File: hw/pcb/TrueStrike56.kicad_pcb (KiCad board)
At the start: 2 copper layers, 278.9 x 138.4 mm, 202 parts, among them SW1 SW_Push, U1 ProMicro, U10 4053, U2 74HC4051, U3 74HC4051, U4 74HC4051, U5 74HC4051, U6 74HC4051, U7 74HC4051, U8 74HC4051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

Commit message: Add mounting holes and plates, MCU cover
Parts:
- added REF**: MountingHole_3.5mm, MountingHole:MountingHole_3.5mm, F.Cu at (112.0, 58.3)
- added REF**: MountingHole_3.5mm, MountingHole:MountingHole_3.5mm, F.Cu at (250.3, 78.7)
- added REF**: MountingHole_3.5mm, MountingHole:MountingHole_3.5mm, F.Cu at (323.6, 58.3)
- added REF**: MountingHole_3.5mm, MountingHole:MountingHole_3.5mm, F.Cu at (162.2, 134.6)
- added REF**: MountingHole_3.5mm, MountingHole:MountingHole_3.5mm, F.Cu at (273.4, 134.6)
- added REF**: MountingHole_3.5mm, MountingHole:MountingHole_3.5mm, F.Cu at (100.5, 117.7)
- added REF**: MountingHole_3.5mm, MountingHole:MountingHole_3.5mm, F.Cu at (335.2, 117.7)
- added REF**: MountingHole_3.5mm, MountingHole:MountingHole_3.5mm, F.Cu at (185.3, 78.7)

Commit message: Add logo+model name+rev #, set LCSC Part # for PCBA order
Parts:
- added G***: LOGO, LOGO, B.Cu at (319.0, 119.1)
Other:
- board text added: "Rev.1"
- board text added: "TrueStrike56"

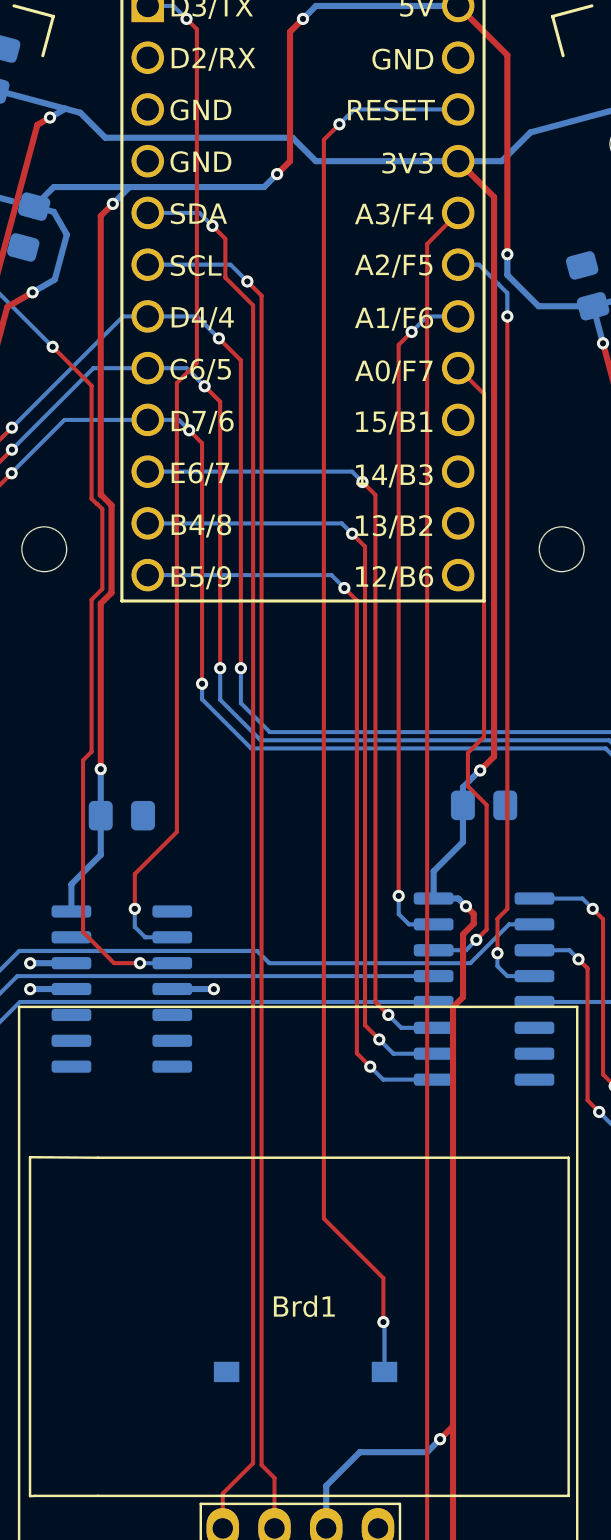
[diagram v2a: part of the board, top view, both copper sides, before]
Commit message: Update PCB and production files for PCBA
Changed RESET tactile switch to JLCPCB PCBA compatible part
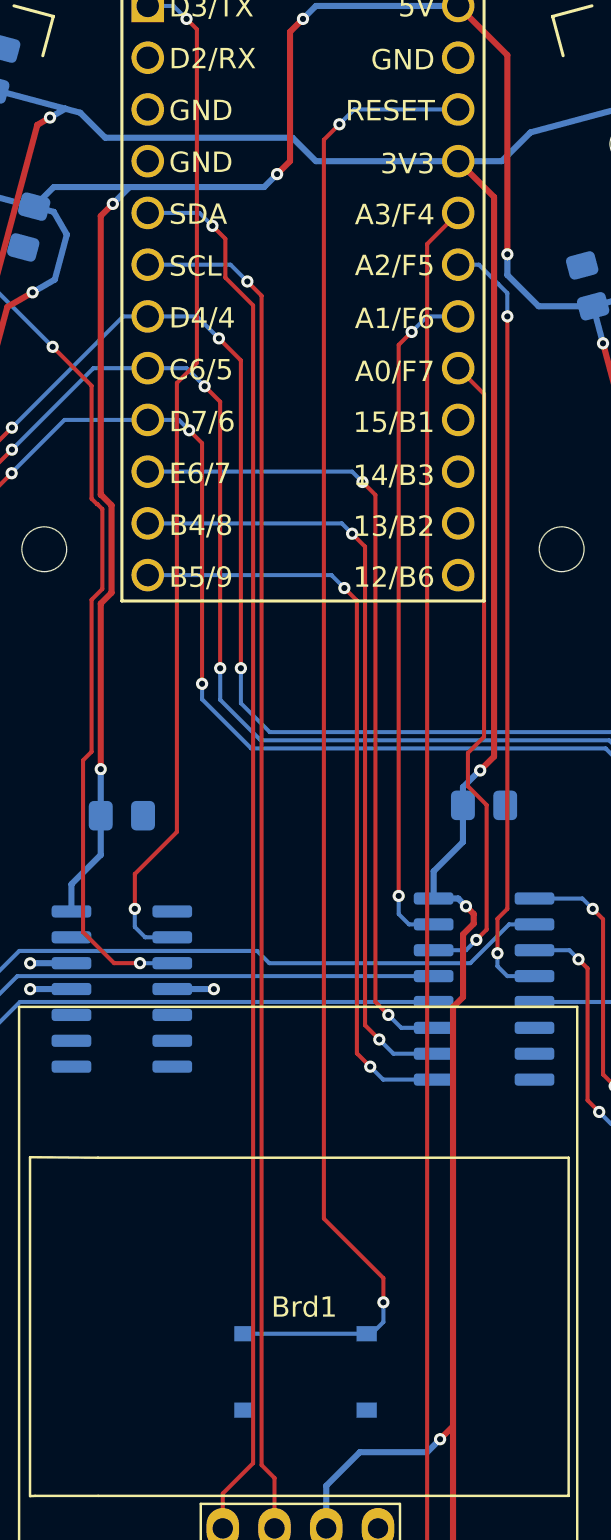
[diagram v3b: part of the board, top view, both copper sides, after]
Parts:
- SW1: footprint Button_Switch_SMD:SW_Tactile_SPST_NO_Straight_CK_PTS636Sx25SMTRLFS -> Button_Switch_SMD:SW_Push_1P1T_XKB_TS-1187A
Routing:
- net RESET: track 68.9 -> 73.5 mm
